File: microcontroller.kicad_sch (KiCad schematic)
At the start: 44 parts, among them J10 ${MANUFACTURER PART NUMBER}, J11 ${MANUFACTURER PART NUMBER}, J8 ${MANUFACTURER PART NUMBER}, J9 ${MANUFACTURER PART NUMBER}, U1 ${MANUFACTURER PART NUMBER}, U5 ${MANUFACTURER PART NUMBER}, U6 USBLC6-2P6, Y1 ${FREQUENCY}

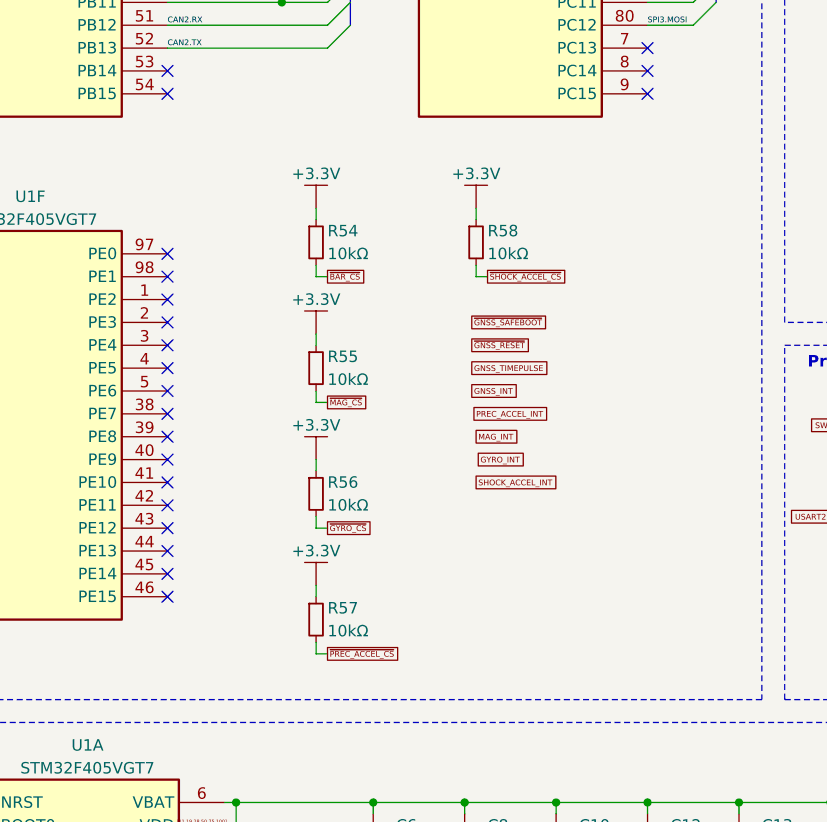
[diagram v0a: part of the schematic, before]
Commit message: Place pullup resistors for SPI bus
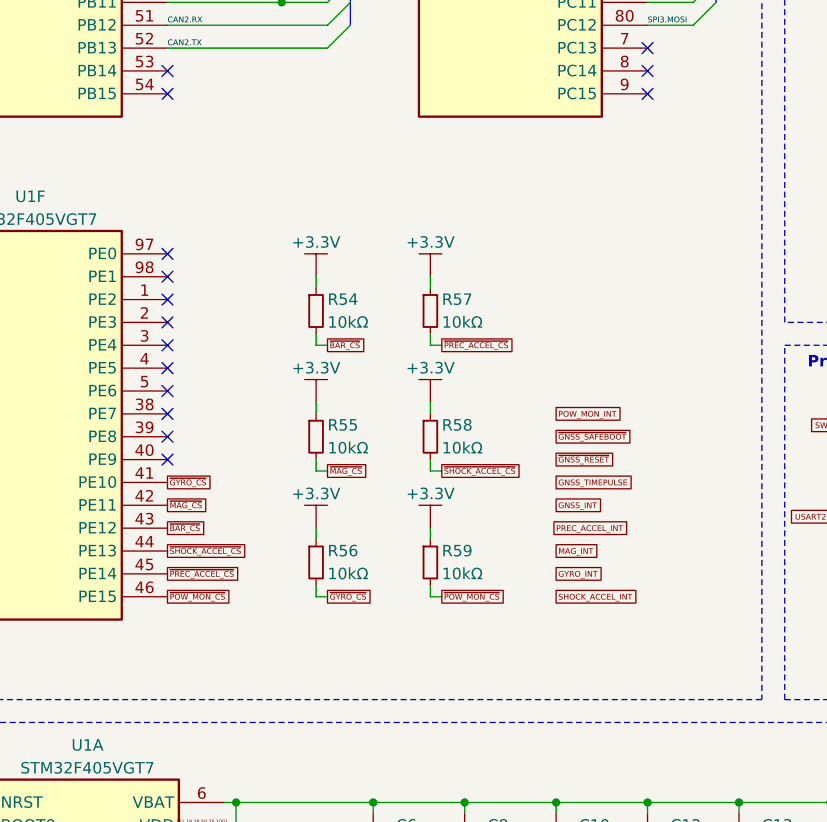
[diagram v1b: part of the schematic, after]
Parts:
- added R59: ${RESISTANCE}, passive_resistor:R_0603_Density_Nominal, symbol passive_resistor:CRCW060310K0FKEAHP
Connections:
- net +3.3V: now also R59.1
- net ~{BAR_CS}: now also U1.43 (PE12)
- net ~{GYRO_CS}: now also U1.41 (PE10)
- net ~{MAG_CS}: now also U1.42 (PE11)
- net ~{PREC_ACCEL_CS}: now also U1.45 (PE14)
- net ~{SHOCK_ACCEL_CS}: now also U1.44 (PE13)
- net ~{POW_MON_CS}: now reaches U1.46 (PE15)
- net ~{POW_MON_CS}: now also R59.2
- no-connect marks 55 -> 49
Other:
- moved on the sheet: R54, R55, R56, R57, R58
